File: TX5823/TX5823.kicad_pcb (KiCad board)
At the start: 2 copper layers, 72 parts, among them IC1 ATMEGA328P-A, IC2 ATTINY13A-SS, P1 Akku_in, P2 ISP, P3 Mavlink, Q3 MOSFET_N, SW1 SW_PUSH, SW2 SW_PUSH, U2 TPS54531, U3 TPS7A7200RGT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

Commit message: an Layout gearbeitet
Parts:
- C23, R25, R31: moved to F.Cu
- moved R25 30.9 mm to (86.6, 48.3), turned to 180 degrees
- moved R31 11.8 mm to (102.4, 44.6)
- moved R24 6.69 mm to (108.5, 23.6), turned to 90 degrees
- moved R23 4.46 mm to (112.3, 30.8)
- moved D6 3.91 mm to (90.4, 25.2)
- moved C29 3.89 mm to (108.5, 27.6), turned to 90 degrees
- moved R22 3.54 mm to (91.0, 27.4), turned to 90 degrees
- moved C23 2.20 mm to (88.4, 26.9)
- moved C25 2.06 mm to (84.2, 30.2)
- moved C11 1.56 mm to (103.9, 65.0), turned to 0 degrees
- moved R21 1.20 mm to (76.8, 22.6)
- moved C24 1.17 mm to (76.1, 27.1)
- moved C14 1.10 mm to (111.8, 58.2)
- moved Q3 1.10 mm to (113.3, 34.7)
- moved C27 1.00 mm to (92.5, 54.7)
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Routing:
- net +5V: track 0.00 -> 200.0 mm, vias 0 -> 24
- net GND: track 0.00 -> 183.5 mm, vias 0 -> 33
- net +3.3V: track 0.00 -> 55.5 mm, vias 0 -> 5
- net /RESET: track 0.00 -> 47.8 mm, vias 0 -> 3
- net /IR_LED-: track 0.00 -> 42.7 mm, vias 0 -> 1
- net /MOSI: track 0.00 -> 28.6 mm, vias 0 -> 1
- net /PWM_in: track 0.00 -> 27.8 mm, vias 0 -> 2
- net /AUDIO_IN_TX: track 0.00 -> 25.1 mm, vias 0 -> 1
- net Net-(IC2-Pad3): track 0.00 -> 22.0 mm, vias 0 -> 2
- net Net-(P3-Pad5): track 0.00 -> 18.9 mm, vias 0 -> 2
- net /SCK: track 0.00 -> 17.6 mm, vias 0 -> 1
- net /MISO: track 0.00 -> 17.5 mm, vias 0 -> 1
- net Net-(U4-Pad7): track 0.00 -> 16.3 mm
- net Net-(IC2-Pad5): track 0.00 -> 13.5 mm, vias 0 -> 1
- net +12V: track 0.00 -> 13.3 mm
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- added copper zone on F.Cu, net +3.3V
- added copper zone on Signal, net +3.3V
- added copper zone on F.Cu, net +5V
- added copper zone on Signal, net +5V
- added copper zone on F.Cu, net GND
- added copper zone on GND, net GND
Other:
- copper layers 2 -> 4
- net class Default: clearance 0.254 -> 0.2
- rule trace_clearance: 0.254 -> 0.2
- rule trace_min: 0.254 -> 0.1524
- rule via_min_drill: 0.508 -> 0.4
- rule via_min_size: 0.889 -> 0.8

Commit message: Layout fertig bis auf startup teil
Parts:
- added D1: DIODE, toni:POWERDI5, F.Cu at (107.7, 55.3)
- C25, C37, R30: moved to F.Cu
- U7: footprint toni:TSSOP-20_4.4x6.5mm_Pitch0.65mm_EP -> toni:TSSOP-28_4.4x9.7mm_Pitch0.65mm_EP
- moved C35 7.82 mm to (102.4, 39.6)
- moved C34 6.81 mm to (96.7, 35.2), turned to 180 degrees
- moved C30 5.85 mm to (85.7, 39.7), turned to 180 degrees
- moved C37 5.57 mm to (93.8, 41.9)
- moved C33 4.90 mm to (96.7, 36.6), turned to 180 degrees
- moved C25 4.41 mm to (88.6, 29.9), turned to 0 degrees
- moved RP1 3.26 mm to (97.5, 32.5)
- moved R30 2.48 mm to (90.1, 41.5), turned to 90 degrees
- moved R29 1.97 mm to (102.3, 33.5)
- moved C5 1.97 mm to (114.1, 63.7)
- moved C8 1.97 mm to (116.1, 63.7)
- moved C3 1.97 mm to (102.4, 61.8)
- moved C1 1.97 mm to (99.2, 61.8)
- moved C11 1.97 mm to (104.7, 66.8)
- moved C14 1.97 mm to (112.6, 60.0)
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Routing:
- net GND: track 183.5 -> 240.1 mm, vias 33 -> 36
- net +5V: track 200.0 -> 248.6 mm, vias 24 -> 25
- net /VIDEO_OUT_OSD: track 0.00 -> 32.0 mm, vias 0 -> 3
- net +3.3V: track 55.5 -> 81.7 mm
- net /VSYNC: track 2.00 -> 25.9 mm, vias 0 -> 2
- net /LOS: track 0.00 -> 10.8 mm
- net Net-(C14-Pad1): track 8.51 -> 19.0 mm
- net /SSOSD-IN: track 0.00 -> 10.4 mm, vias 0 -> 1
- net /RESET: track 47.8 -> 57.5 mm, vias 3 -> 4
- net /MOSI: track 28.6 -> 37.8 mm, vias 1 -> 3
- net Net-(C36-Pad1): track 0.00 -> 9.08 mm
- net /SCK: track 17.6 -> 26.6 mm, vias 1 -> 3
- net Net-(C35-Pad1): track 0.00 -> 8.78 mm
- net Net-(C37-Pad2): track 0.00 -> 7.13 mm, vias 0 -> 1
- net /VIDEO_IN_OSD: track 0.00 -> 6.99 mm
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- added copper zone on B.Cu, net GND

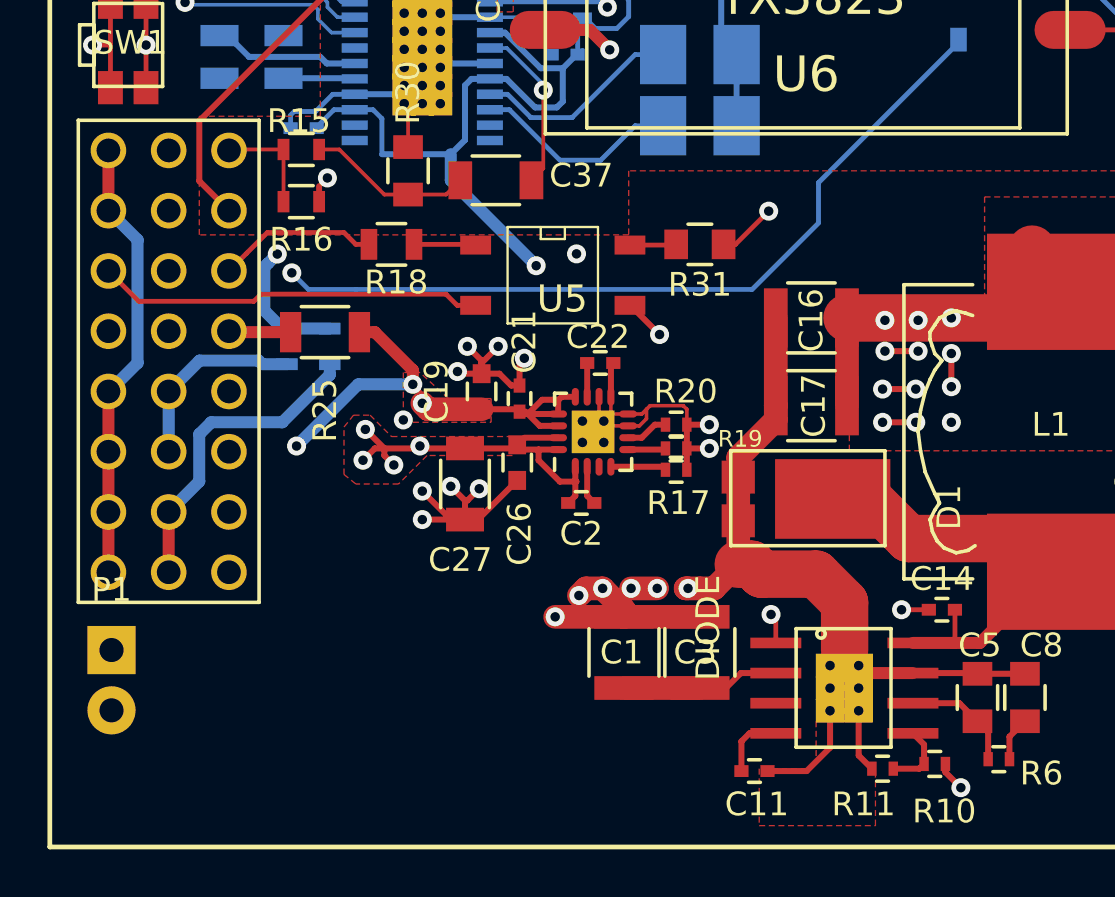
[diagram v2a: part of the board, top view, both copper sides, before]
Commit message: zusätzlicher LDO für OSD hinzugefügt Softstart hinzugefügt
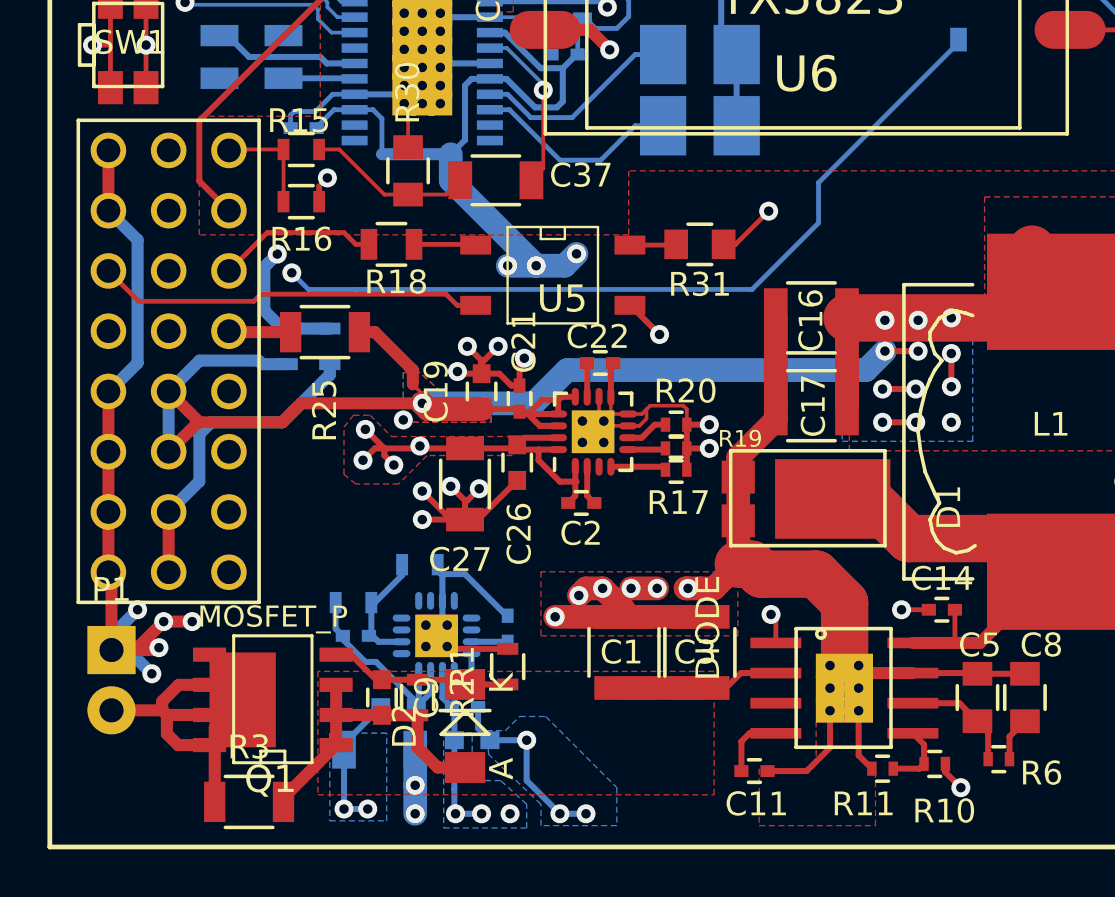
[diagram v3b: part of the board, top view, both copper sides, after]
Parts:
- added C10: 220pF, Capacitors_SMD:C_0402, B.Cu at (87.9, 61.1)
- added C12: 1uF, Capacitors_SMD:C_0603, B.Cu at (89.7, 64.1)
- added C13: 10uF, Capacitors_SMD:C_1206, B.Cu at (88.9, 65.9)
- added C4: 1uF, Capacitors_SMD:C_0603, B.Cu at (92.8, 65.5)
- added C6: 100nF, Capacitors_SMD:C_0402, B.Cu at (92.5, 64.1)
- added C7: 100nF, Capacitors_SMD:C_0402, B.Cu at (94.3, 60.8)
- added C9: C, Capacitors_SMD:C_0603, F.Cu at (89.0, 63.7)
- added D2: ZENER, Diodes_SMD:Diode-MiniMELF_Standard, F.Cu at (92.5, 64.9)
- added Q1: MOSFET_P, toni:SO8_WITH_EP, F.Cu at (84.4, 63.8)
- added R1: R, Resistors_SMD:R_0603, F.Cu at (94.3, 62.4)
- added R2: R, Resistors_SMD:R_0603, F.Cu at (90.5, 63.7)
- added R3: R, Resistors_SMD:R_1206, F.Cu at (83.4, 68.1)
- added R4: 280k, Resistors_SMD:R_0603, B.Cu at (87.8, 59.7)
- added R5: 30,9k, Resistors_SMD:R_0603, B.Cu at (90.6, 58.1)
- added U1: TPS7A7200RGT, toni:QFN-16-1EP_3x3mm_Pitch0.5mm, B.Cu at (91.3, 61.1)
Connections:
- C1 pad 1: /Akku+ -> /Akku+_SS
- C16 pad 1: +5V -> /5,2V
- C17 pad 1: +5V -> /5,2V
- C19 pad 1: +5V -> /5,2V
- C21 pad 1: +5V -> /5,2V
- C3 pad 1: /Akku+ -> /Akku+_SS
- L1 pad 2: +5V -> /5,2V
- R10 pad 1: +5V -> /5,2V
- R14 pad 1: +5V -> /5,2V
- R25 pad 1: +5V -> /5,2V
- U2 pad 2: /Akku+ -> /Akku+_SS
- U3 pad 12: +5V -> /5,2V
- U3 pad 13: +5V -> /5,2V
- U3 pad 14: +5V -> /5,2V
- U4 pad 14: +5V -> /5,2V
- U4 pad 17: +5V -> /5,2V
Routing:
- net /5,2V: track 0.00 -> 147.2 mm, vias 0 -> 18
- net +5V: track 248.6 -> 176.6 mm, vias 25 -> 11
- net GND: track 240.1 -> 279.4 mm, vias 36 -> 46
- net /Akku+_SS: track 0.00 -> 19.7 mm
- net /Akku+: track 6.66 -> 14.5 mm
- net Net-(C9-Pad1): track 0.00 -> 7.75 mm
- net Net-(C10-Pad2): track 0.00 -> 5.15 mm
- net Net-(C7-Pad1): track 0.00 -> 1.52 mm
- added copper zone on B.Cu, net /5,2V
- added copper zone on F.Cu, net /5,2V
- added copper zone on Signal, net /5,2V
- added copper zone on F.Cu, net /Akku+_SS
- removed copper zone on F.Cu, net +5V
- removed copper zone on Signal, net +5V

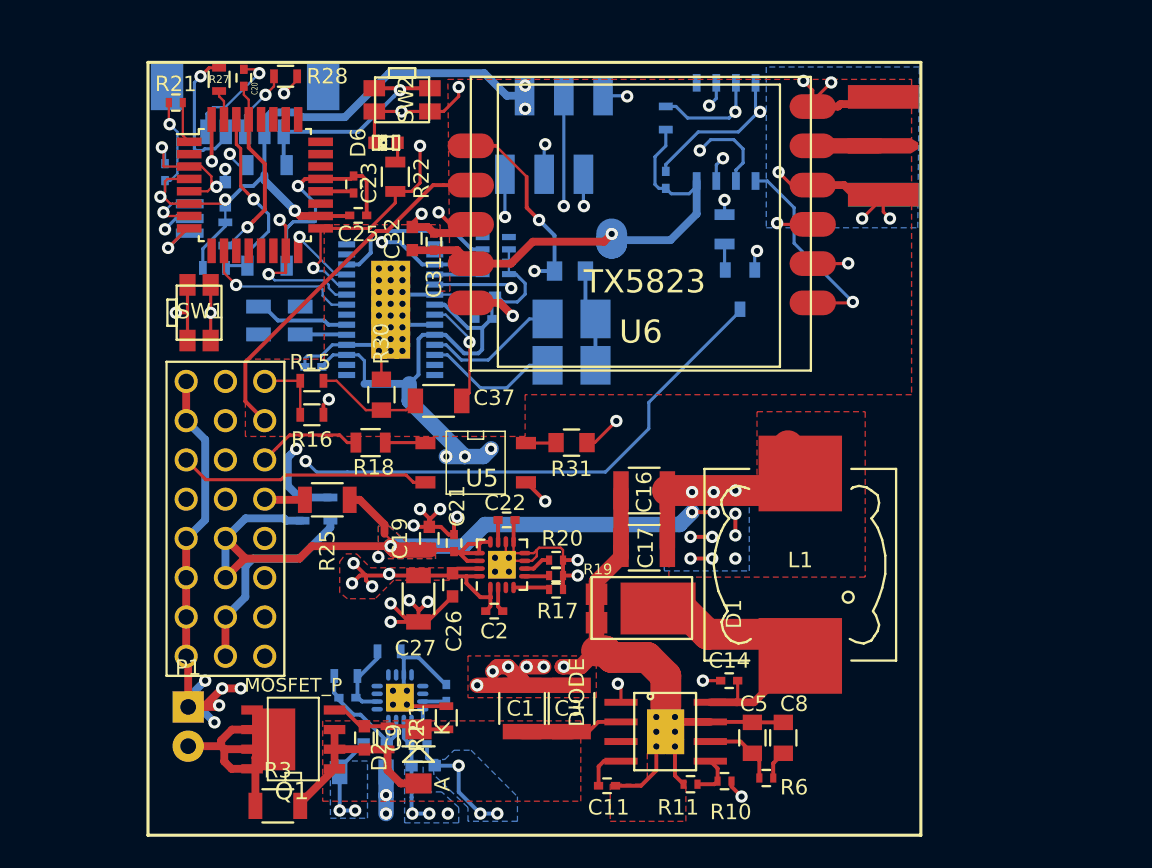
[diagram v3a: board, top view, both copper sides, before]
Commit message: Verbindungspunkte für 12V BuckBoost Aufsteckplatine hinzugefügt
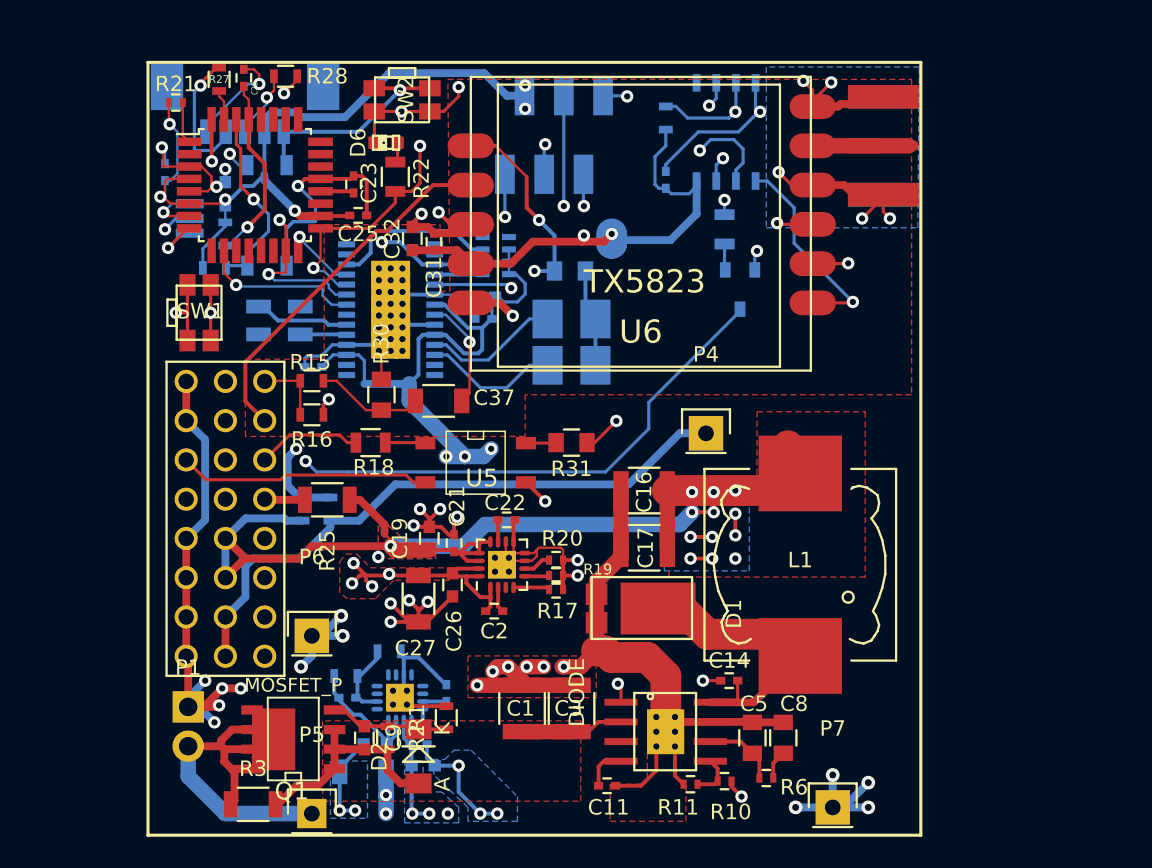
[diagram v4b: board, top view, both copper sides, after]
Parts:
- added P4: CONN_01X01, Pin_Headers:Pin_Header_Straight_1x01, F.Cu at (111.1, 44.0)
- added P5: CONN_01X01, Pin_Headers:Pin_Header_Straight_1x01, F.Cu at (85.6, 68.6)
- added P6: CONN_01X01, Pin_Headers:Pin_Header_Straight_1x01, F.Cu at (85.6, 57.1)
- added P7: CONN_01X01, Pin_Headers:Pin_Header_Straight_1x01, F.Cu at (119.3, 68.2)
- moved R3 1.60 mm to (81.8, 68.0)
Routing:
- net +12V: track 13.3 -> 40.0 mm
- net GND: track 279.4 -> 295.9 mm, vias 46 -> 53
- net /Akku+: track 14.5 -> 25.0 mm
- net +3.3V: track 81.7 -> 84.0 mm, vias 5 -> 6
- net /Akku+_SS: track 19.7 -> 21.3 mm
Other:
- net class Default: clearance 0.2 -> 0.19
- rule trace_clearance: 0.2 -> 0.19
